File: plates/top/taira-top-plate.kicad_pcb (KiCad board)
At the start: 2 copper layers, 151.5 x 121.2 mm, 41 parts, among them SW1 SW_Push, SW10 SW_Push, SW11 SW_Push, SW12 SW_Push, SW13 SW_Push, SW14 SW_Push, SW15 SW_Push, SW16 SW_Push, SW17 SW_Push, SW18 SW_Push, SW19 SW_Push, SW2 SW_Push, SW20 SW_Push, SW21 SW_Push, SW22 SW_Push, SW23 SW_Push, SW24 SW_Push, SW25 SW_Push, SW26 SW_Push, SW27 SW_Push, SW28 SW_Push, SW29 SW_Push, SW3 SW_Push, SW30 SW_Push, SW31 SW_Push, SW32 SW_Push, SW33 SW_Push, SW4 SW_Push, SW5 SW_Push, SW6 SW_Push, SW7 SW_Push, SW8 SW_Push, SW9 SW_Push

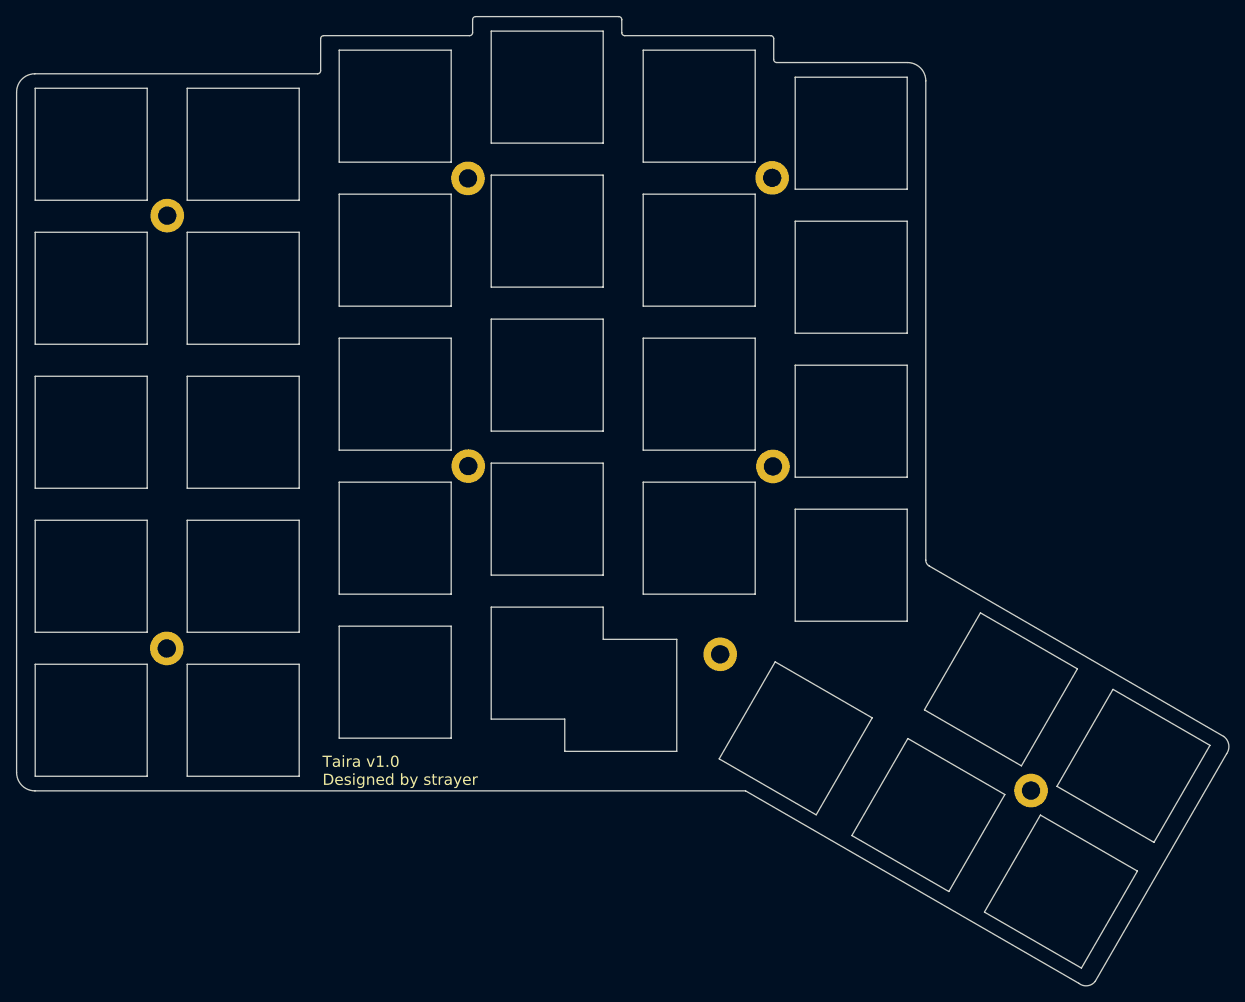
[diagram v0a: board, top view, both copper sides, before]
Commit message: kicad 4 -> 10
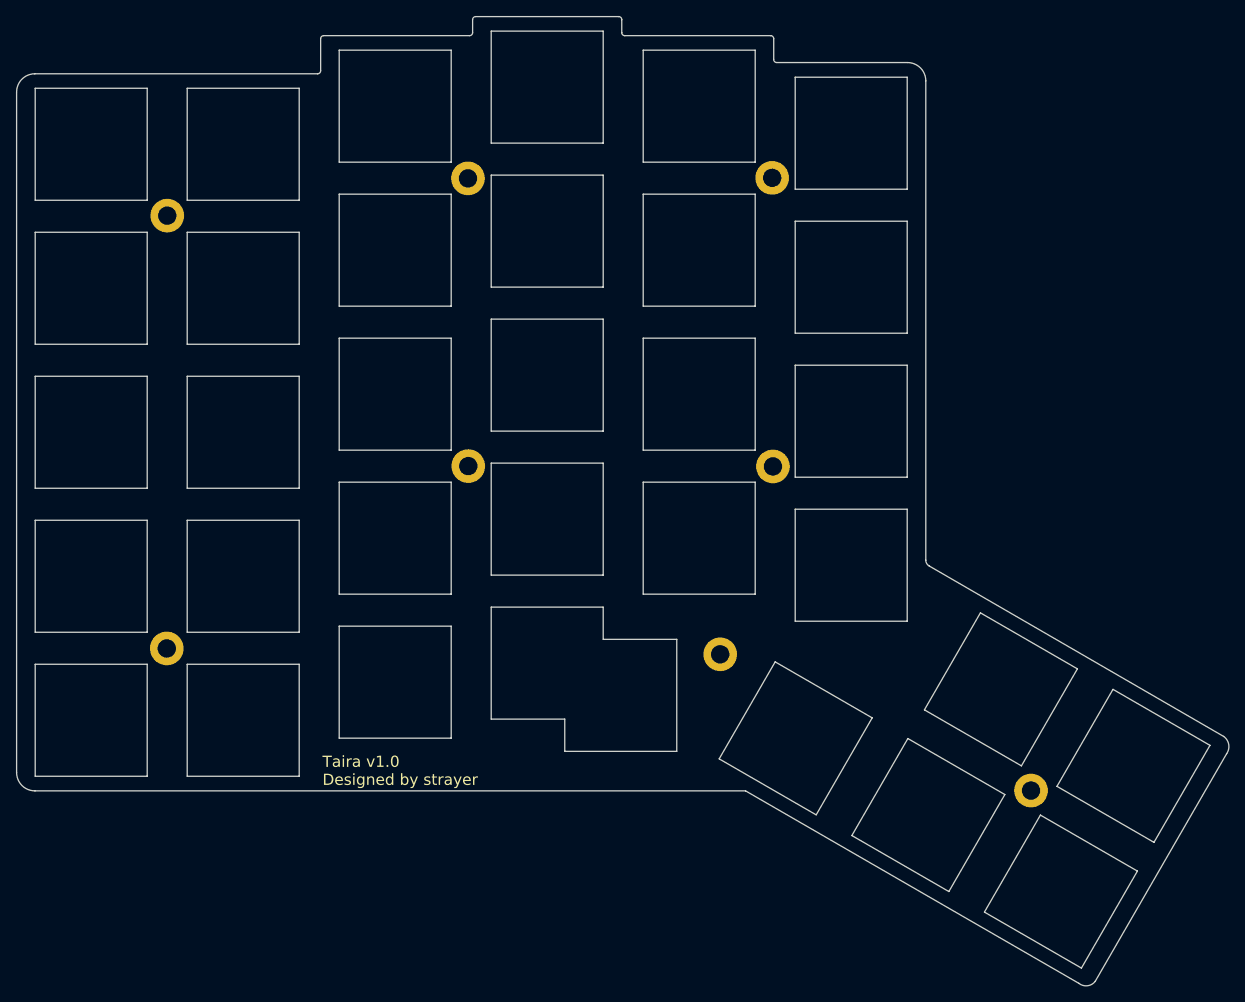
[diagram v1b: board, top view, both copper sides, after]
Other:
- net class Default removed
